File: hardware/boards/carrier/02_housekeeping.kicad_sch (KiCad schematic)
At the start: 15 parts, among them SW1 SKSCLCE010, U1 STM32C092GCU7

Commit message: checkpoint carrier sourcing and zone state
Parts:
- U1: LCSC (none) -> C44847705
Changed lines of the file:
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@@
 			)
 		)
-		(property "LCSC" ""
+		(property "LCSC" "C44847705"
 			(at 76.2 68.58 0)
 			(hide yes)

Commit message: assign carrier LCSC assembly parts
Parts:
- C11, C12, C14, C17: LCSC (none) -> C14663; MPN (none) -> CC0603KRX7R9BB104; Manufacturer (none) -> YAGEO
- C13: LCSC (none) -> C19666; MPN (none) -> CL10A475KO8NNNC; Manufacturer (none) -> Samsung Electro-Mechanics
- J2: LCSC (none) -> C32713271; MPN (none) -> HX PZ2.54-1x5P ZZ; Manufacturer (none) -> hanxia
- R24, R25: LCSC (none) -> C4190; MPN (none) -> 0603WAF2201T5E; Manufacturer (none) -> UNI-ROYAL (Uniroyal Elec)
- R28, R30: LCSC (none) -> C25804; MPN (none) -> 0603WAF1002T5E; Manufacturer (none) -> UNI-ROYAL (Uniroyal Elec)
- R31: LCSC (none) -> C25803; MPN (none) -> 0603WAF1003T5E; Manufacturer (none) -> UNI-ROYAL (Uniroyal Elec)
- R32: LCSC (none) -> C22775; MPN (none) -> 0603WAF1000T5E; Manufacturer (none) -> UNI-ROYAL (Uniroyal Elec)
- U1: LCSC C44847705 -> C49361604

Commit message: use stocked MCU and termination resistor parts
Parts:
- U1: value STM32C092GCU7 -> STM32C092GCU6; LCSC C49361604 -> C44847705; MPN STM32C092GCU7 -> STM32C092GCU6
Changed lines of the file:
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@@
 			)
 		)
-		(property "Value" "STM32C092GCU7"
+		(property "Value" "STM32C092GCU6"
 			(at 74.168 74.422 90)
 			(show_name no)
@@
 			)
 		)
-		(property "MPN" "STM32C092GCU7"
+		(property "MPN" "STM32C092GCU6"
 			(at 76.2 68.58 0)
 			(hide yes)
@@
 			)
 		)
-		(property "LCSC" "C49361604"
+		(property "LCSC" "C44847705"
 			(at 76.2 68.58 0)
 			(hide yes)

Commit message: clean up carrier assembly BOM metadata
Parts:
- J2: Population (none) -> DNP; now not fitted
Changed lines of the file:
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@@
 		(on_board yes)
 		(in_pos_files yes)
-		(dnp no)
+		(dnp yes)
 		(fields_autoplaced yes)
 		(property "Reference" "J2"
@@
 			(at 85.09 144.78 0)
 			(hide yes)
+			(show_name no)
+			(do_not_autoplace no)
+			(effects
+				(font
+					(size 1.27 1.27)
+				)
+			)
+		)
+		(property "Population" "DNP"
+			(at 85.09 144.78 0)
+			(hide yes)

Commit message: consolidate carrier assembly parts
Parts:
- SW1: Population (none) -> DNP; now not fitted
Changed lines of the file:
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@@
 		(on_board yes)
 		(in_pos_files yes)
-		(dnp no)
+		(dnp yes)
 		(property "Reference" "SW1"
 			(at 154.94 104.648 0)
@@
 			(at 154.94 107.95 0)
 			(hide yes)
+			(show_name no)
+			(do_not_autoplace no)
+			(effects
+				(font
+					(size 1.27 1.27)
+				)
+			)
+		)
+		(property "Population" "DNP"
+			(at 154.94 107.95 0)
+			(hide yes)

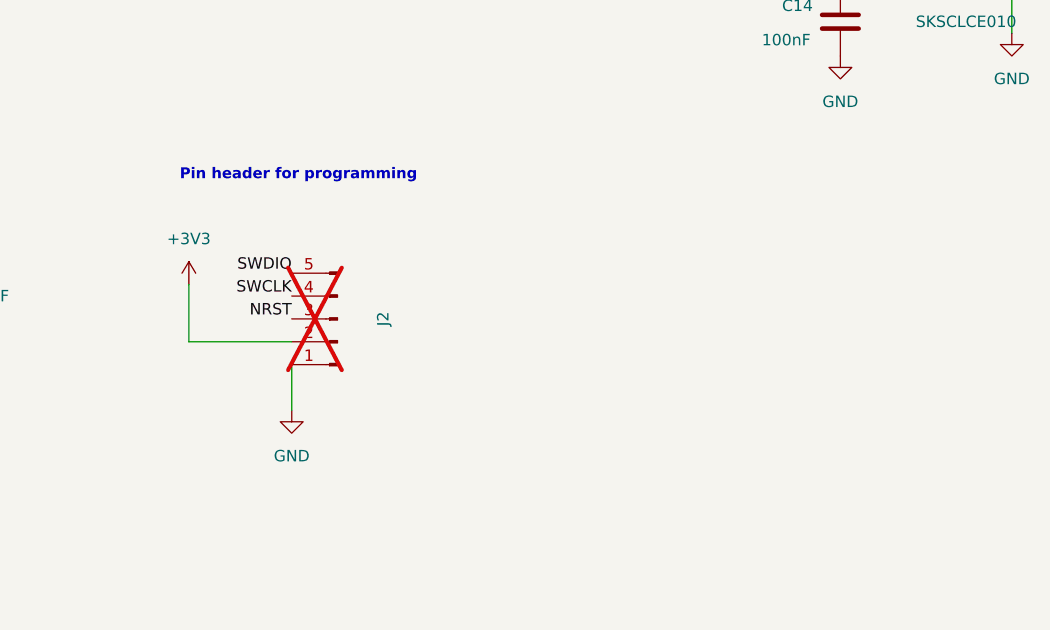
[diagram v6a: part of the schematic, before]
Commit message: replace SWD header with Tag-Connect
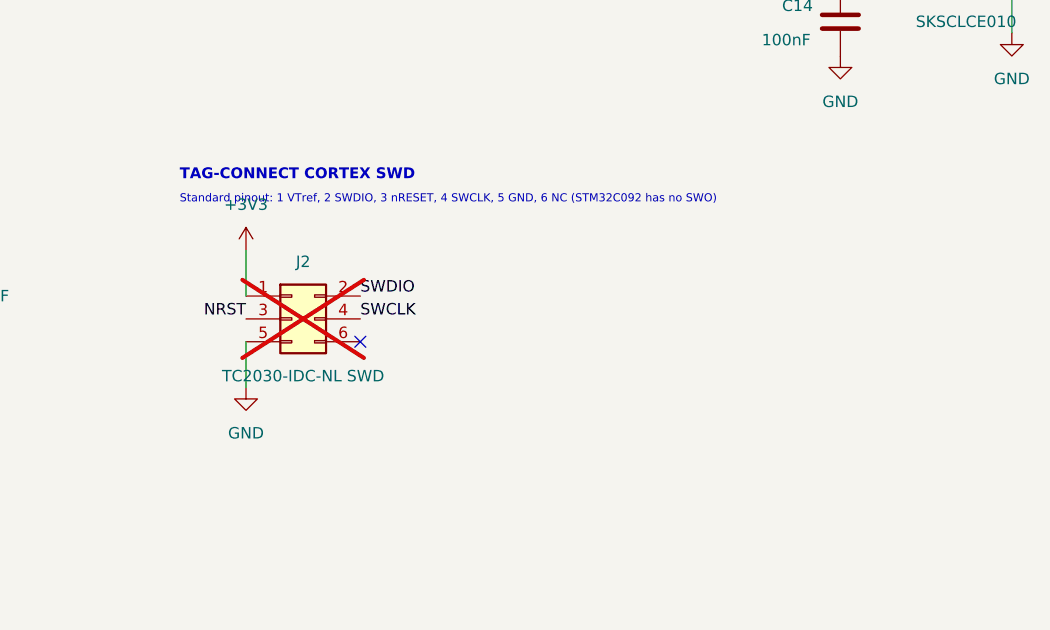
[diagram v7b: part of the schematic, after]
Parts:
- J2: value (none) -> TC2030-IDC-NL SWD; footprint Connector_PinHeader_2.54mm:PinHeader_1x05_P2.54mm_Vertical -> Connector:Tag-Connect_TC2030-IDC-NL_2x03_P1.27mm_Vertical; symbol Connector:Conn_01x05_Pin -> Connector_Generic:Conn_02x03_Odd_Even; LCSC C32713271 -> (none); MPN HX PZ2.54-1x5P ZZ -> TC2030-IDC-NL; Manufacturer hanxia -> Tag-Connect
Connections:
- net +3V3: now also J2.1 (Pin_1); no longer J2.2 (Pin_2)
- net GND: now also J2.5 (Pin_5); no longer J2.1 (Pin_1)
- net SWDIO: now also J2.2 (Pin_2); no longer J2.5 (Pin_5)
- no-connect marks 13 -> 14
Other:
- note added: "Standard pinout: 1 VTref, 2 SWDIO, 3 nRESET, 4 SWCLK, 5 GND, 6 NC (STM32C092 has no SWO)"
- note added: "TAG-CONNECT CORTEX SWD"
- note removed: "Pin header for programming"
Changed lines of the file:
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@@
 		)
 	)
-	(text "Pin header for programming"
+	(text "TAG-CONNECT CORTEX SWD"
 		(exclude_from_sim no)
 		(at 67.564 129.54 0)
@@
 				(size 1.2 1.2)
 				(bold yes)
+			)
+			(justify left bottom)
+		)
+	)
+	(text "Standard pinout: 1 VTref, 2 SWDIO, 3 nRESET, 4 SWCLK, 5 GND, 6 NC (STM32C092 has no SWO)"
+		(exclude_from_sim no)
+		(at 67.564 132.08 0)
+		(effects
+			(font
+				(size 0.9 0.9)
 			)
 			(justify left bottom)
@@
 		(at 93.98 83.82)
 	)
+	(no_connect
+		(at 87.63 147.32)
+	)
 	(wire
 		(pts
-			(xy 80.01 154.94) (xy 80.01 149.86)
+			(xy 74.93 152.4) (xy 74.93 147.32)
 		)
 		(stroke
@@
 	(wire
 		(pts
-			(xy 68.58 140.97) (xy 68.58 147.32)
+			(xy 74.93 137.16) (xy 74.93 142.24)
 		)
 		(stroke
@@
 	(wire
 		(pts
-			(xy 68.58 147.32) (xy 80.01 147.32)
+			(xy 359.41 109.22) (xy 359.41 105.41)
 		)
 		(stroke
@@
 		)
 	)
-	(wire
-		(pts
-			(xy 359.41 109.22) (xy 359.41 105.41)
-		)
-		(stroke
-			(width 0)
-			(type default)
-		)
-	)
 	(label "PD_IRQ"
 		(at 113.03 63.5 0)
@@
 	)
 	(label "NRST"
-		(at 80.01 144.78 180)
+		(at 74.93 144.78 180)
 		(effects
 			(font
@@
 	)
 	(label "SWCLK"
-		(at 80.01 142.24 180)
-		(effects
-			(font
-				(size 1.27 1.27)
-			)
-			(justify right bottom)
+		(at 87.63 144.78 0)
+		(effects
+			(font
+				(size 1.27 1.27)
+			)
+			(justify left bottom)
 		)
 	)
@@
 	)
 	(label "SWDIO"
-		(at 80.01 139.7 180)
-		(effects
-			(font
-				(size 1.27 1.27)
-			)
-			(justify right bottom)
+		(at 87.63 142.24 0)
+		(effects
+			(font
+				(size 1.27 1.27)
+			)
+			(justify left bottom)
 		)
 	)
@@
 	(symbol
 		(lib_id "power:GND")
-		(at 80.01 154.94 0)
+		(at 74.93 152.4 0)
 		(unit 1)
 		(body_style 1)
@@
 		(fields_autoplaced yes)
 		(property "Reference" "#PWR016"
-			(at 80.01 161.29 0)
+			(at 74.93 158.75 0)
 			(hide yes)
 			(show_name no)
@@
 		)
 		(property "Value" "GND"
-			(at 80.01 160.02 0)
+			(at 74.93 157.48 0)
 			(show_name no)
 			(do_not_autoplace no)
@@
 		)
 		(property "Footprint" ""
-			(at 80.01 154.94 0)
+			(at 74.93 152.4 0)
 			(hide yes)
 			(show_name no)
@@
 		)
 		(property "Datasheet" ""
-			(at 80.01 154.94 0)
+			(at 74.93 152.4 0)
 			(hide yes)
 			(show_name no)
@@
 		)
 		(property "Description" "Power symbol creates a global label with name \"GND\" , ground"
-			(at 80.01 154.94 0)
+			(at 74.93 152.4 0)
 			(hide yes)
 			(show_name no)
@@
 	)
 	(symbol
-		(lib_id "Connector:Conn_01x05_Pin")
-		(at 85.09 144.78 180)
+		(lib_id "Connector_Generic:Conn_02x03_Odd_Even")
+		(at 80.01 144.78 0)
 		(unit 1)
 		(body_style 1)
@@
 		(fields_autoplaced yes)
 		(property "Reference" "J2"
-			(at 90.17 144.78 90)
-			(show_name no)
-			(do_not_autoplace no)
-			(effects
-				(font
-					(size 1.27 1.27)
-				)
-			)
-		)
-		(property "Value" ""
-			(at 87.63 144.78 90)
-			(show_name no)
-			(do_not_autoplace no)
-			(effects
-				(font
-					(size 1.27 1.27)
-				)
-			)
-		)
-		(property "Footprint" "Connector_PinHeader_2.54mm:PinHeader_1x05_P2.54mm_Vertical"
-			(at 85.09 144.78 0)
-			(hide yes)
-			(show_name no)
-			(do_not_autoplace no)
-			(effects
-				(font
-					(size 1.27 1.27)
-				)
-			)
-		)
-		(property "Datasheet" ""
-			(at 85.09 144.78 0)
-			(hide yes)
-			(show_name no)
-			(do_not_autoplace no)
-			(effects
-				(font
-					(size 1.27 1.27)
-				)
-			)
-		)
-		(property "Description" "Generic connector, single row, 01x05, script generated"
-			(at 85.09 144.78 0)
-			(hide yes)
-			(show_name no)
-			(do_not_autoplace no)
-			(effects
-				(font
-					(size 1.27 1.27)
-				)
-			)
-		)
-		(property "MPN" "HX PZ2.54-1x5P ZZ"
-			(at 85.09 144.78 0)
-			(hide yes)
-			(show_name no)
-			(do_not_autoplace no)
-			(effects
-				(font
-					(size 1.27 1.27)
-				)
-			)
-		)
-		(property "Manufacturer" "hanxia"
-			(at 85.09 144.78 0)
-			(hide yes)
-			(show_name no)
-			(do_not_autoplace no)
-			(effects
-				(font
-					(size 1.27 1.27)
-				)
-			)
-		)
-		(property "LCSC" "C32713271"
-			(at 85.09 144.78 0)
+			(at 81.28 138.43 0)
+			(show_name no)
+			(do_not_autoplace no)
+			(effects
+				(font
+					(size 1.27 1.27)
+				)
+			)
+		)
+		(property "Value" "TC2030-IDC-NL SWD"
+			(at 81.28 151.13 0)
+			(show_name no)
+			(do_not_autoplace no)
+			(effects
+				(font
+					(size 1.27 1.27)
+				)
+			)
+		)
+		(property "Footprint" "Connector:Tag-Connect_TC2030-IDC-NL_2x03_P1.27mm_Vertical"
+			(at 80.01 144.78 0)
+			(hide yes)
+			(show_name no)
+			(do_not_autoplace no)
+			(effects
+				(font
+					(size 1.27 1.27)
+				)
+			)
+		)
+		(property "Datasheet" "https://www.tag-connect.com/wp-content/uploads/bsk-pdf-manager/2019/12/TC2030-IDC-NL-Datasheet-Rev-B.pdf"
+			(at 80.01 144.78 0)
+			(hide yes)
+			(show_name no)
+			(do_not_autoplace no)
+			(effects
+				(font
+					(size 1.27 1.27)
+				)
+			)
+		)
+		(property "Description" "6-pin no-legs Tag-Connect Cortex SWD programming and debug interface"
+			(at 80.01 144.78 0)
+			(hide yes)
+			(show_name no)
+			(do_not_autoplace no)
+			(effects
+				(font
+					(size 1.27 1.27)
+				)
+			)
+		)
+		(property "MPN" "TC2030-IDC-NL"
+			(at 80.01 144.78 0)
+			(hide yes)
+			(show_name no)
+			(do_not_autoplace no)
+			(effects
+				(font
+					(size 1.27 1.27)
+				)
+			)
+		)
+		(property "Manufacturer" "Tag-Connect"
+			(at 80.01 144.78 0)
+			(hide yes)
+			(show_name no)
+			(do_not_autoplace no)
+			(effects
+				(font
+					(size 1.27 1.27)
+				)
+			)
+		)
+		(property "LCSC" ""
+			(at 80.01 144.78 0)
 			(hide yes)
 			(show_name no)
@@
 		)
 		(property "Population" "DNP"
-			(at 85.09 144.78 0)
+			(at 80.01 144.78 0)
 			(hide yes)
 			(show_name no)
@@
 		)
 		(pin "4"
+		)
+		(pin "6"
 		)
 		(instances
@@
 	(symbol
 		(lib_id "power:+3V3")
-		(at 68.58 140.97 0)
+		(at 74.93 137.16 0)
 		(unit 1)
 		(body_style 1)
@@
 		(fields_autoplaced yes)
 		(property "Reference" "#PWR022"
-			(at 68.58 144.78 0)
+			(at 74.93 140.97 0)
 			(hide yes)
 			(show_name no)
@@
 		)
 		(property "Value" "+3V3"
-			(at 68.58 135.89 0)
+			(at 74.93 132.08 0)
 			(show_name no)
 			(do_not_autoplace no)
@@
 		)
 		(property "Footprint" ""
-			(at 68.58 140.97 0)
+			(at 74.93 137.16 0)
 			(hide yes)
 			(show_name no)
@@
 		)
 		(property "Datasheet" ""
-			(at 68.58 140.97 0)
+			(at 74.93 137.16 0)
 			(hide yes)
 			(show_name no)
@@
 		)
 		(property "Description" "Power symbol creates a global label with name \"+3V3\""
-			(at 68.58 140.97 0)
-			(hide yes)
-			(show_name no)
+			(at 74.93 137.16 0)
+			(hide yes)
+			(show_name no)

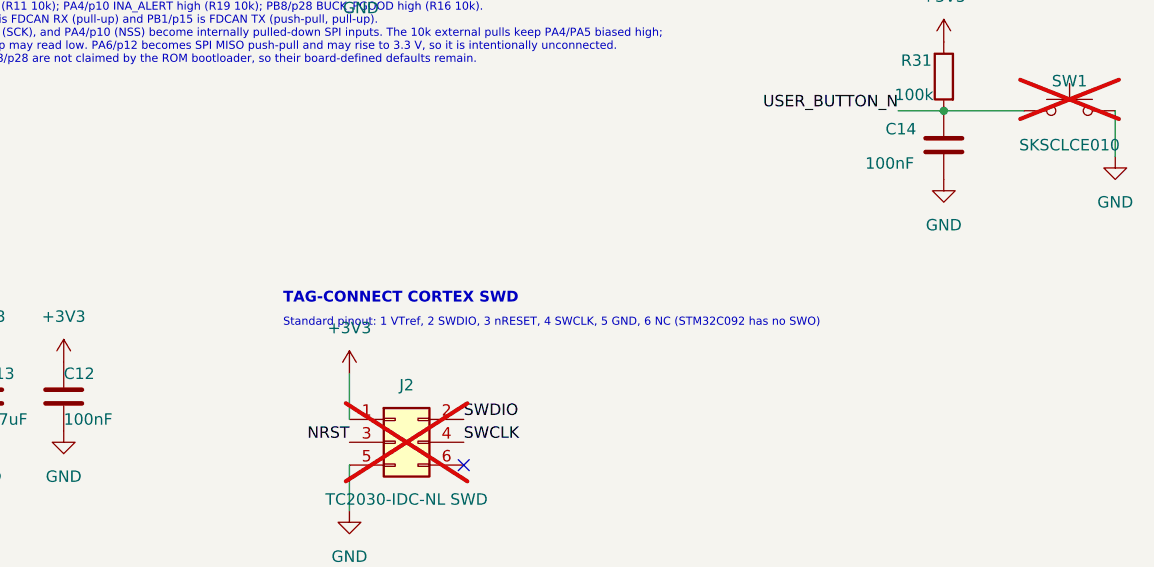
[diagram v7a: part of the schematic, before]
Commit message: checkpoint carrier layout before rerouting
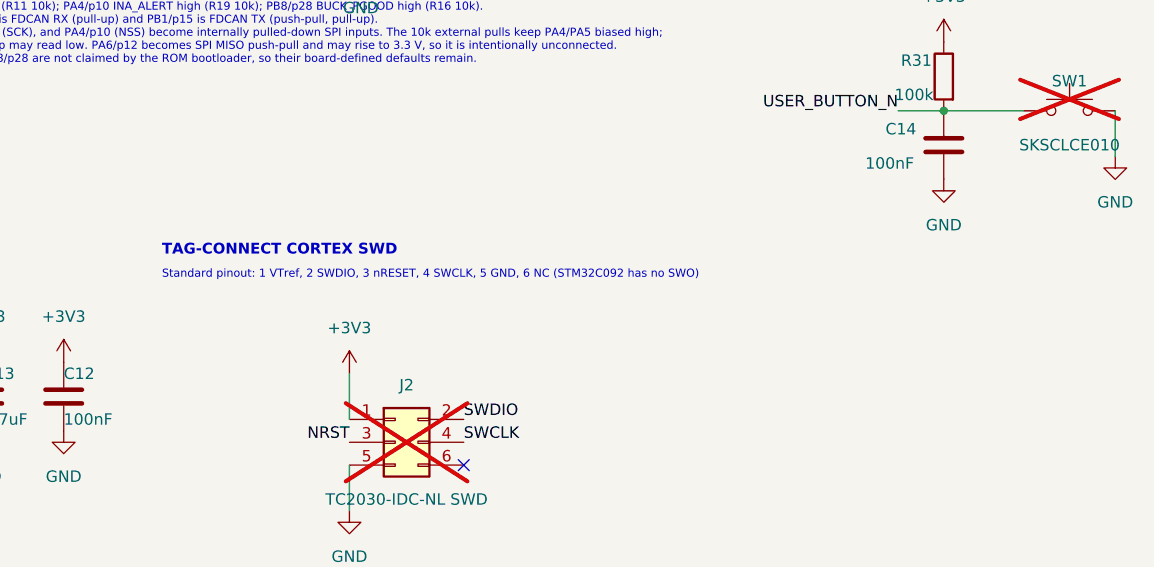
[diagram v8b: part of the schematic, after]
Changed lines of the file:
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@@
 		(comment 2 "Future 240 W capability requires a new hardware revision")
+	)
+	(text "Standard pinout: 1 VTref, 2 SWDIO, 3 nRESET, 4 SWCLK, 5 GND, 6 NC (STM32C092 has no SWO)"
+		(exclude_from_sim no)
+		(at 54.102 126.746 0)
+		(effects
+			(font
+				(size 0.9 0.9)
+			)
+			(justify left bottom)
+		)
 	)
 	(text "FACTORY ROM FDCAN RECOVERY\nCAN_RX = PB0/pin 14; CAN_TX = PB1/pin 15."
@@
 	(text "TAG-CONNECT CORTEX SWD"
 		(exclude_from_sim no)
-		(at 67.564 129.54 0)
+		(at 54.102 124.206 0)
 		(effects
 			(font
 				(size 1.2 1.2)
 				(bold yes)
-			)
-			(justify left bottom)
-		)
-	)
-	(text "Standard pinout: 1 VTref, 2 SWDIO, 3 nRESET, 4 SWCLK, 5 GND, 6 NC (STM32C092 has no SWO)"
-		(exclude_from_sim no)
-		(at 67.564 132.08 0)
-		(effects
-			(font
-				(size 0.9 0.9)
 			)
 			(justify left bottom)
@@
 	)
 	(no_connect
+		(at 87.63 147.32)
+	)
+	(no_connect
 		(at 58.42 71.12)
 	)
@@
 		(at 93.98 83.82)
 	)
-	(no_connect
-		(at 87.63 147.32)
-	)
 	(wire
